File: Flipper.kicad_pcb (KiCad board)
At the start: 2 copper layers, 34 x 67 mm, 13 parts, among them IC1 DWM1000, J1 Conn_01x08_Socket, J2 Conn_01x10_Socket

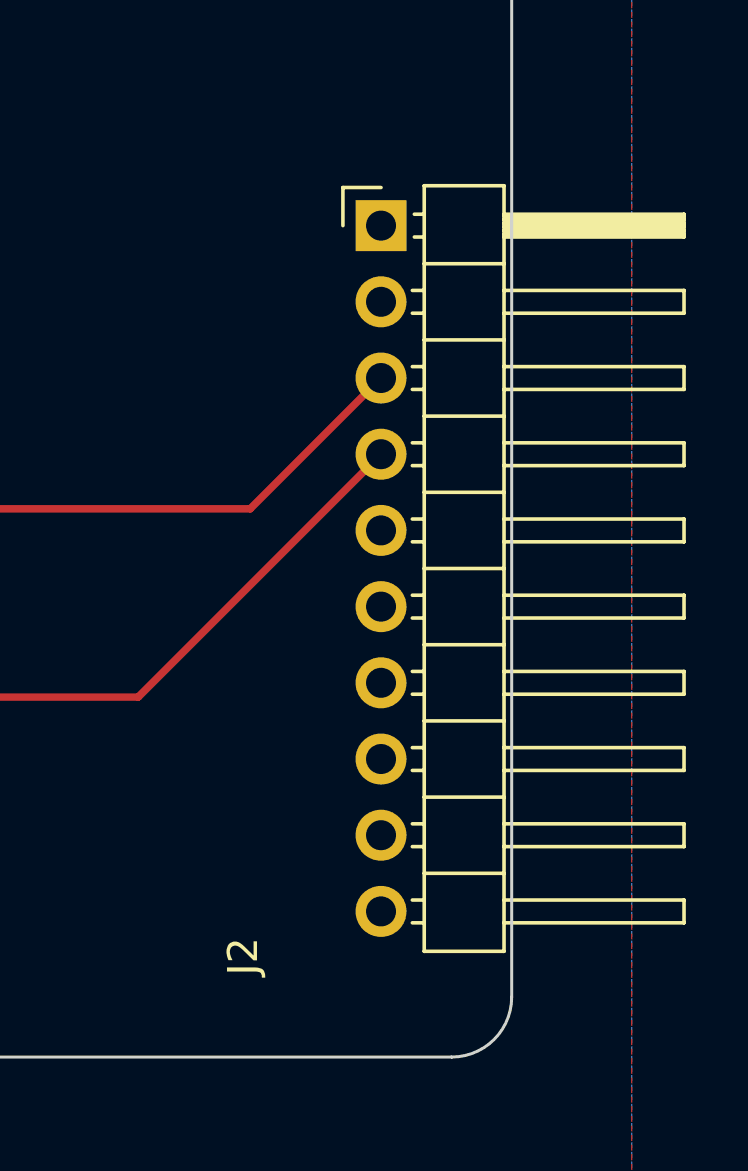
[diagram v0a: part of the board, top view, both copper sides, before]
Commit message: Update Flipper PCB
Update of the measurements between pins
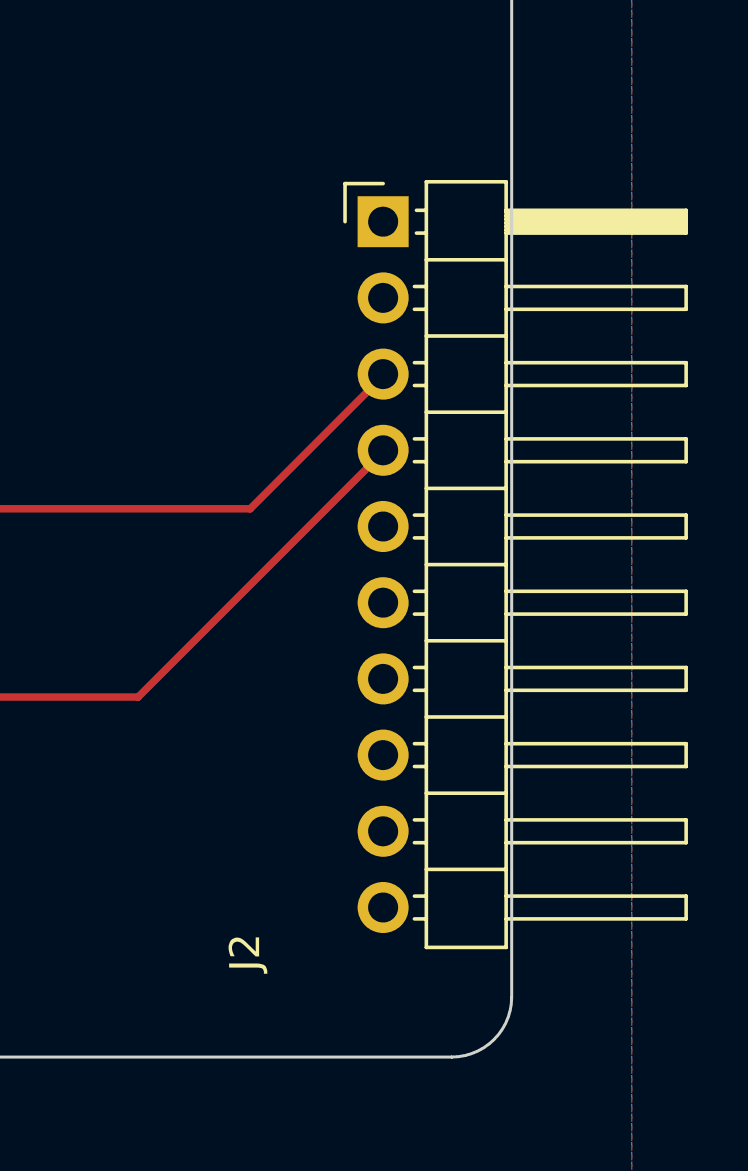
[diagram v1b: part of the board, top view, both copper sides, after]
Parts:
- moved J2 0.15 mm to (153.7, 102.2)
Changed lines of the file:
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@@
   )
   (footprint "Connector_PinHeader_2.54mm:PinHeader_1x10_P2.54mm_Horizontal" (layer "F.Cu")
-    (at 153.6446 102.2858)
+    (at 153.715 102.155)
     (descr "Through hole angled pin header, 1x10, 2.54mm pitch, 6mm pin length, single row")
     (tags "Through hole angled pin header THT 1x10 2.54mm single row")
@@
     (stroke (width 0.1) (type default)) (layer "Edge.Cuts"))
   (dimension (type aligned) (layer "F.SilkS")
-    (pts (xy 154.4066 86.1568) (xy 154.35 101))
-    (height -19.287992)
-    (gr_text "14.8433 mm" (at 171.866165 93.645084 89.78152114) (layer "F.SilkS")
-      (effects (font (size 1.5 1.5) (thickness 0.3)))
-    )
-    (format (prefix "") (suffix "") (units 3) (units_format 1) (precision 4))
-    (style (thickness 0.2) (arrow_length 1.27) (text_position_mode 0) (extension_height 0.58642) (extension_offset 0.5) keep_text_aligned)
-  )
-  (dimension (type aligned) (layer "F.SilkS")
     (pts (xy 127 63) (xy 126.7 129.9))
     (height 16.376324)
@@
   )
   (dimension (type aligned) (layer "F.SilkS")
-    (pts (xy 153.5684 102.1588) (xy 153.5684 84.4042))
-    (height 33.8524)
-    (gr_text "17.7546 mm" (at 185.6208 93.2815 90) (layer "F.SilkS")
-      (effects (font (size 1.5 1.5) (thickness 0.3)))
+    (pts (xy 153.68 84.37) (xy 153.715 102.155))
+    (height -20.925327)
+    (gr_text "17.7850 mm" (at 175.772784 93.219057 270.1127551) (layer "F.SilkS")
+      (effects (font (size 1 1) (thickness 0.15)))
     )
     (format (prefix "") (suffix "") (units 3) (units_format 1) (precision 4))
-    (style (thickness 0.2) (arrow_length 1.27) (text_position_mode 0) (extension_height 0.58642) (extension_offset 0.5) keep_text_aligned)
+    (style (thickness 0.15) (arrow_length 1.27) (text_position_mode 0) (extension_height 0.58642) (extension_offset 0.5) keep_text_aligned)
   )
   (dimension (type aligned) (layer "F.SilkS")
